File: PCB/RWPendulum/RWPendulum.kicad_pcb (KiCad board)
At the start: 2 copper layers, 119.6 x 59.2 mm, 17 parts, among them IC1 L7805CV, J1 Screw_Terminal_01x02, J2 Conn_01x06_Pin, J3 Conn_01x04_Pin, J4 Screw_Terminal_01x02, SW1 SW_SPST, SW2 SW_Push, U2 ESP32-DEVKIT-V1

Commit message: Atualizado design da PCB e arquivos gerber + drill
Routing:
- net +5V: track 21.0 -> 5.71 mm, vias 2 -> 0
- net /DRIVER_PWM1: track 120.8 -> 118.1 mm
- net +12V: track 30.3 -> 28.3 mm
- net /DRIVER_PWM2: track 106.8 -> 107.5 mm

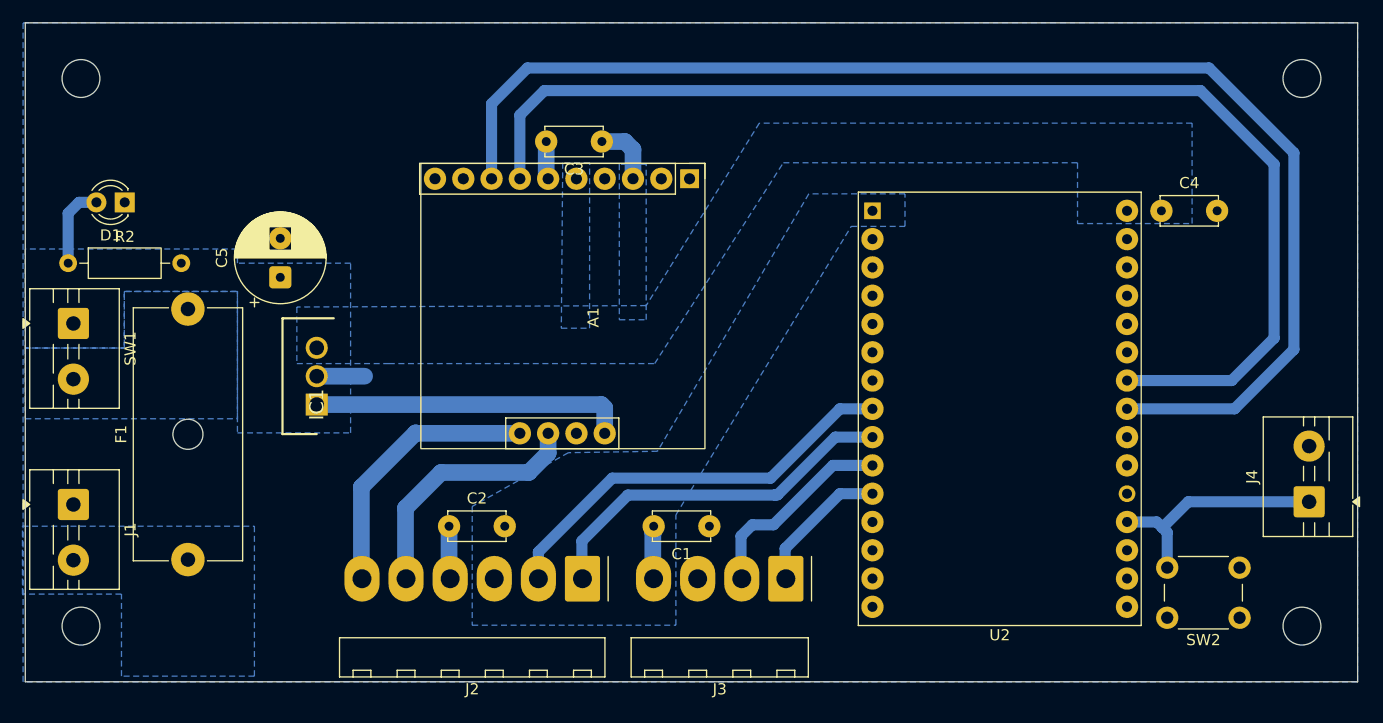
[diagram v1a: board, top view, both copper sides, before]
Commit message: PCB: Rev. 1 - Gabriel Tumang - 22/01/2026
Mudando pino do botão EN_CONTROL para 27 no lugar do 34 para utilizar função de pullup interno da ESP32,
por consequência, os pinos de PWM p/ o driver foram modvidos para facilitar o roteamento.
Também foram alterados tamanhos dos furos e pads de alguns componentes para tentar minimizar problemas de fabricação.
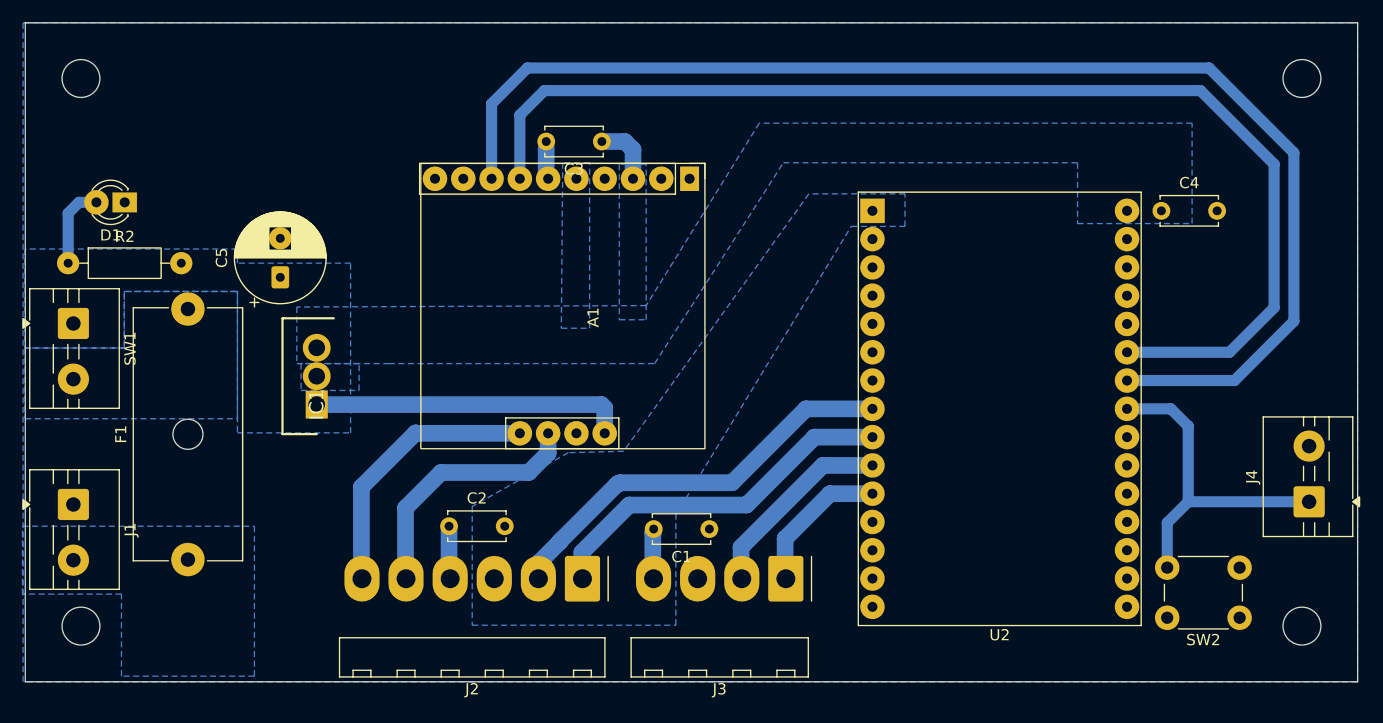
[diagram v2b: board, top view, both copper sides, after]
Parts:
- A1: footprint RWPendulum_Library:MD36A Motor Driver Header -> BibliotecaGT:MD36A Motor Driver Header
- C1, C2, C3, C4: footprint RWPendulum_Library:C_Disc_D5.0mm_W2.5mm_P5.00mm -> Capacitor_THT:C_Disc_D5.0mm_W2.5mm_P5.00mm
- C5: footprint RWPendulum_Library:CP_Radial_D8.0mm_P3.50mm -> Capacitor_THT:CP_Radial_D8.0mm_P3.50mm
- D1: footprint RWPendulum_Library:LED_D3.0mm -> LED_THT:LED_D3.0mm
- F1: footprint RWPendulum_Library:Fuseholder_Cylinder-5x20mm_Schurter_0031_8201_Horizontal_Open -> Fuse:Fuseholder_Cylinder-5x20mm_Schurter_0031_8201_Horizontal_Open
- IC1: footprint RWPendulum_Library:TO255P460X1020X2008-3P -> LibraryLoader:TO255P460X1020X2008-3P
- J1, J4, SW1: footprint RWPendulum_Library:TerminalBlock_MaiXu_MX126-5.0-02P_1x02_P5.00mm -> TerminalBlock:TerminalBlock_MaiXu_MX126-5.0-02P_1x02_P5.00mm
- J2: footprint RWPendulum_Library:Molex_KK-396_A-41792-0006_1x06_P3.96mm_Horizontal -> Connector_Molex:Molex_KK-396_A-41792-0006_1x06_P3.96mm_Horizontal
- J3: footprint RWPendulum_Library:Molex_KK-396_A-41792-0004_1x04_P3.96mm_Horizontal -> Connector_Molex:Molex_KK-396_A-41792-0004_1x04_P3.96mm_Horizontal
- R2: footprint RWPendulum_Library:R_Axial_DIN0207_L6.3mm_D2.5mm_P10.16mm_Horizontal -> Resistor_THT:R_Axial_DIN0207_L6.3mm_D2.5mm_P10.16mm_Horizontal
- SW2: footprint RWPendulum_Library:SW_PUSH_6mm_H4.3mm -> Button_Switch_THT:SW_PUSH_6mm_H4.3mm
- U2: footprint RWPendulum_Library:ESP32-C3-DevKitM-1 -> RF_Module:ESP32-C3-DevKitM-1
- moved C1 0.25 mm to (148.6, 116.5)
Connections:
- U2 pad 19: /BTN_EN_CONTROL -> unconnected-(U2-D34-Pad19)
- U2 pad 23: /DRIVER_PWM1 -> /BTN_EN_CONTROL
- U2 pad 24: /DRIVER_PWM2 -> /DRIVER_PWM1
- U2 pad 25: unconnected-(U2-D27-Pad25) -> /DRIVER_PWM2
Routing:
- net /BTN_EN_CONTROL: track 21.3 -> 30.5 mm
- net GND: track 11.9 -> 7.64 mm
- net /DRIVER_PWM2: track 107.5 -> 104.8 mm
- net /DRIVER_PWM1: track 118.1 -> 115.6 mm
- net /MOTOR_ENC_B: track 33.9 -> 33.3 mm
- net /BASE_ENC_A: track 18.8 -> 18.2 mm
- net /MOTOR_ENC_A: track 40.0 -> 39.4 mm
- net /BASE_ENC_B: track 13.1 -> 13.6 mm
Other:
- board text added: "Rev. 0 - Gabriel Tumang - 20/01/2026 Versão inicial Rev. 1 - Gabriel Tumang - 22/01/2026 Mudando pino do botão EN_CONTROL para 27 no lugar do 34 para utilizar função de pullup interno da ESP32, por consequência, os pinos de PWM p/ o driver foram modvidos para facilitar o roteamento. Também foram alterados tamanhos dos furos e pads de alguns componentes para tentar minimizar problemas de fabricaçã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"
